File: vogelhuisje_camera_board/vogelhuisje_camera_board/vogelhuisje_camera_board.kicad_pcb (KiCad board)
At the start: 2 copper layers, 40 x 84 mm, 23 parts, among them J1 Conn_01x19_Female, J4 Camera Connector, Q2 Q_NMOS_DSG, U1 XC6206-2.8V, U2 XC6206-1.2V

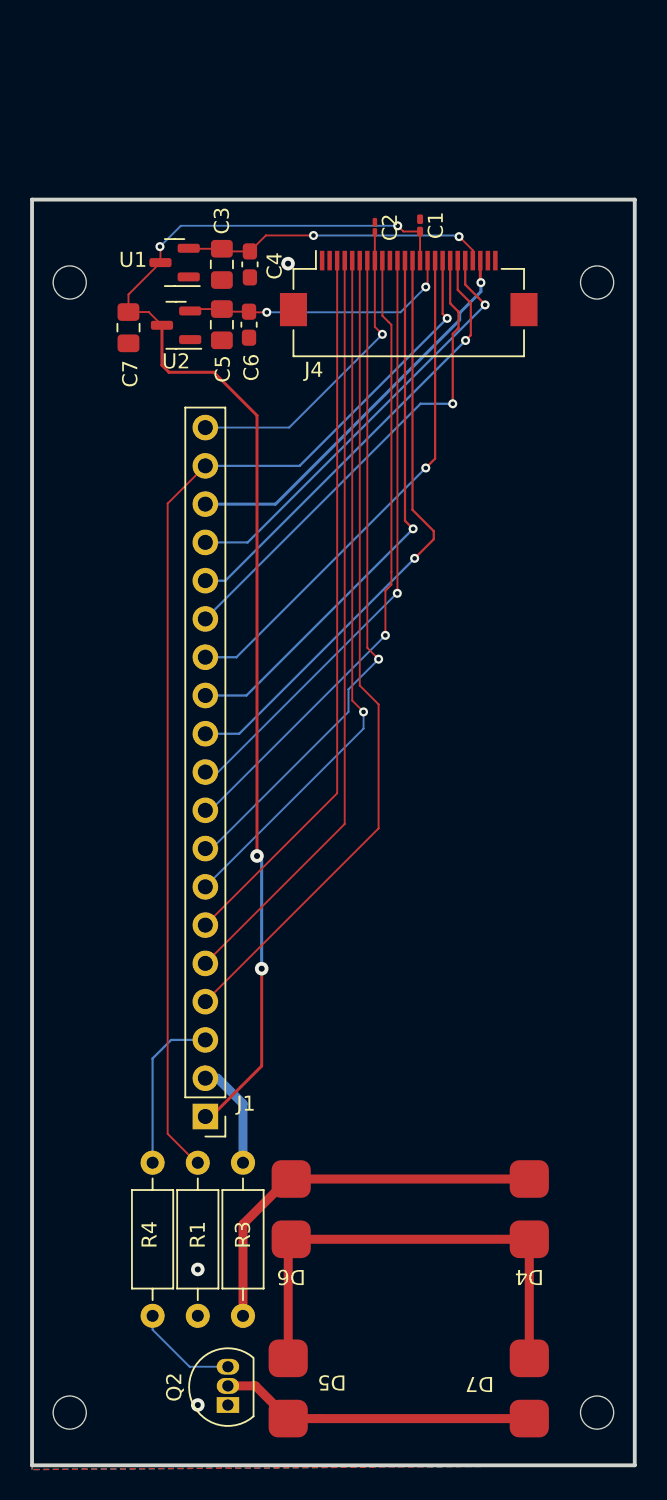
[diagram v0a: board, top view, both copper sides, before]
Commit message: Kicad Changes Tadjiro
Board now supports 3 lipo cells and a motion sensor.
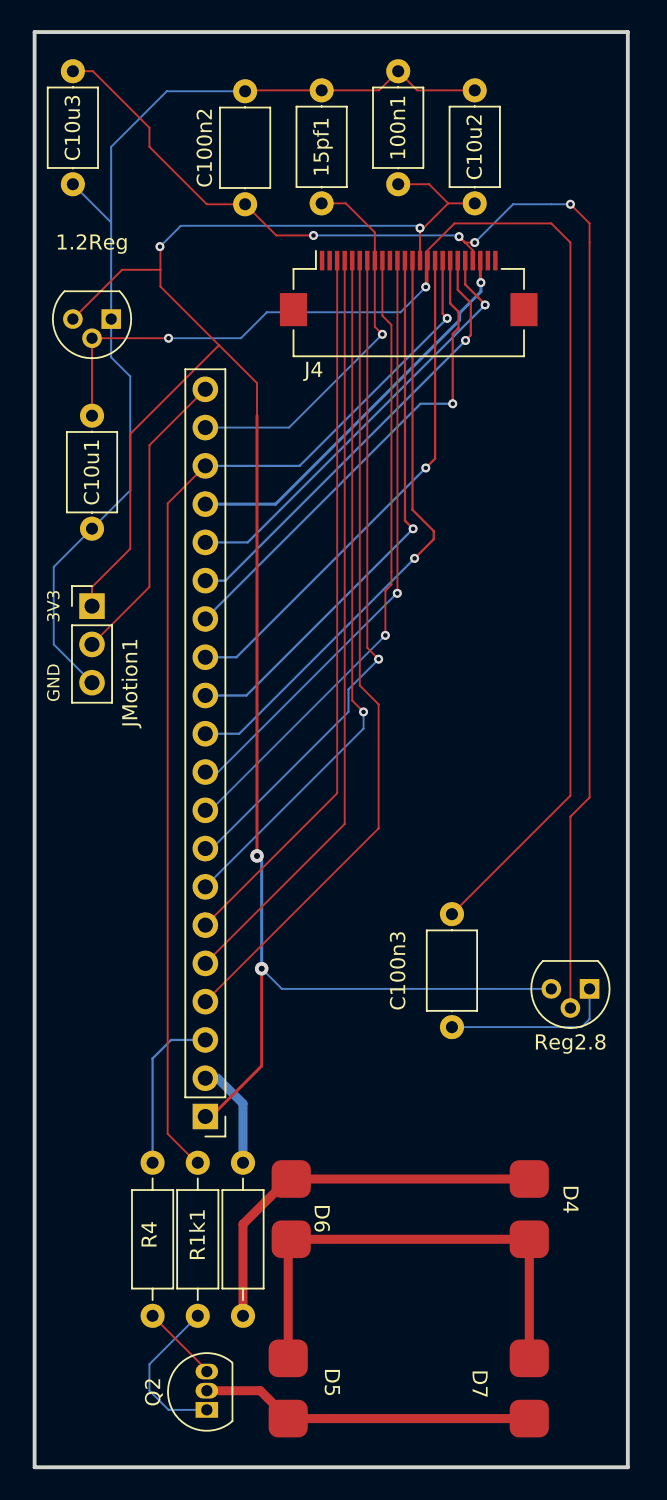
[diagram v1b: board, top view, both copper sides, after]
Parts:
- removed REF** (x4): MountingHole_2.2mm_M2, MountingHole:MountingHole_2.2mm_M2
- added JMotion1: Conn_01x03_Female, Connector_PinHeader_2.54mm:PinHeader_1x03_P2.54mm_Vertical, F.Cu at (94.0, 94.0)
- 1.2Reg: renamed from U2; value XC6206-1.2V -> 1.2V Regulator; footprint Package_TO_SOT_SMD:SOT-23 -> Package_TO_SOT_THT:TO-92
- 100n1: renamed from C1; value 100n -> 100nF; footprint Capacitor_SMD:C_0201_0603Metric_Pad0.64x0.40mm_HandSolder -> Capacitor_THT:C_Axial_L5.1mm_D3.1mm_P7.50mm_Horizontal
- 15pf1: renamed from C2; footprint Capacitor_SMD:C_01005_0402Metric_Pad0.57x0.30mm_HandSolder -> Capacitor_THT:C_Axial_L5.1mm_D3.1mm_P7.50mm_Horizontal
- C100n2: renamed from C4; footprint Capacitor_SMD:C_0603_1608Metric_Pad1.08x0.95mm_HandSolder -> Capacitor_THT:C_Axial_L5.1mm_D3.1mm_P7.50mm_Horizontal
- C100n3: renamed from C6; footprint Capacitor_SMD:C_0603_1608Metric_Pad1.08x0.95mm_HandSolder -> Capacitor_THT:C_Axial_L5.1mm_D3.1mm_P7.50mm_Horizontal
- C10u1: renamed from C5; footprint Capacitor_SMD:C_0805_2012Metric_Pad1.18x1.45mm_HandSolder -> Capacitor_THT:C_Axial_L5.1mm_D3.1mm_P7.50mm_Horizontal
- C10u2: renamed from C7; footprint Capacitor_SMD:C_0805_2012Metric_Pad1.18x1.45mm_HandSolder -> Capacitor_THT:C_Axial_L5.1mm_D3.1mm_P7.50mm_Horizontal
- C10u3: renamed from C3; footprint Capacitor_SMD:C_0805_2012Metric_Pad1.18x1.45mm_HandSolder -> Capacitor_THT:C_Axial_L5.1mm_D3.1mm_P7.50mm_Horizontal
- J1: value Conn_01x19_Female -> Conn_01x20_Female; footprint Connector_PinHeader_2.54mm:PinHeader_1x19_P2.54mm_Vertical -> Connector_PinHeader_2.54mm:PinHeader_1x20_P2.54mm_Vertical
- R1k1: renamed from R1; value 1k -> 1k1
- Reg2.8: renamed from U1; value XC6206-2.8V -> 2.8V regulator; footprint Package_TO_SOT_SMD:SOT-23 -> Package_TO_SOT_THT:TO-92
- moved Reg2.8 55.5 mm to (127.0, 119.4)
- moved C100n3 41.4 mm to (117.9, 114.4)
- moved C10u2 24.4 mm to (119.4, 67.2), turned to 90 degrees
- moved C10u3 16.2 mm to (92.7, 58.5)
- moved C10u1 10.5 mm to (94.0, 81.3)
- moved 100n1 10.3 mm to (114.3, 58.5)
- moved 15pf1 9.75 mm to (109.2, 59.8)
- moved 1.2Reg 4.33 mm to (95.2, 74.9)
- moved C100n2 4.00 mm to (104.1, 67.3), turned to 90 degrees
- moved Q2 1.44 mm to (101.6, 147.3)
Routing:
- net GND: track 0.00 -> 91.6 mm, vias 3 -> 0
- net CSI_2.8V: track 20.5 -> 95.9 mm, vias 2 -> 4
- net CSI_1.2V: track 18.3 -> 91.6 mm
- net 3V3: track 86.5 -> 138.1 mm
- net /Camera Module/Motion_out: track 0.00 -> 20.0 mm
- net /Camera Module/CSI_PCLK: track 21.3 -> 25.6 mm
- net Net-(Q2-Pad3): track 6.94 -> 5.19 mm
- net Net-(D5-Pad1): track 20.9 -> 22.2 mm
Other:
- board size 40 x 84 mm -> 39.4 x 95.2 mm
- board text added: "3V3"
- board text added: "GND"

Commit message: Updated Camera Board
Moved capacitors close to LDO output, corrected capacitor values and ported ground from the main board.
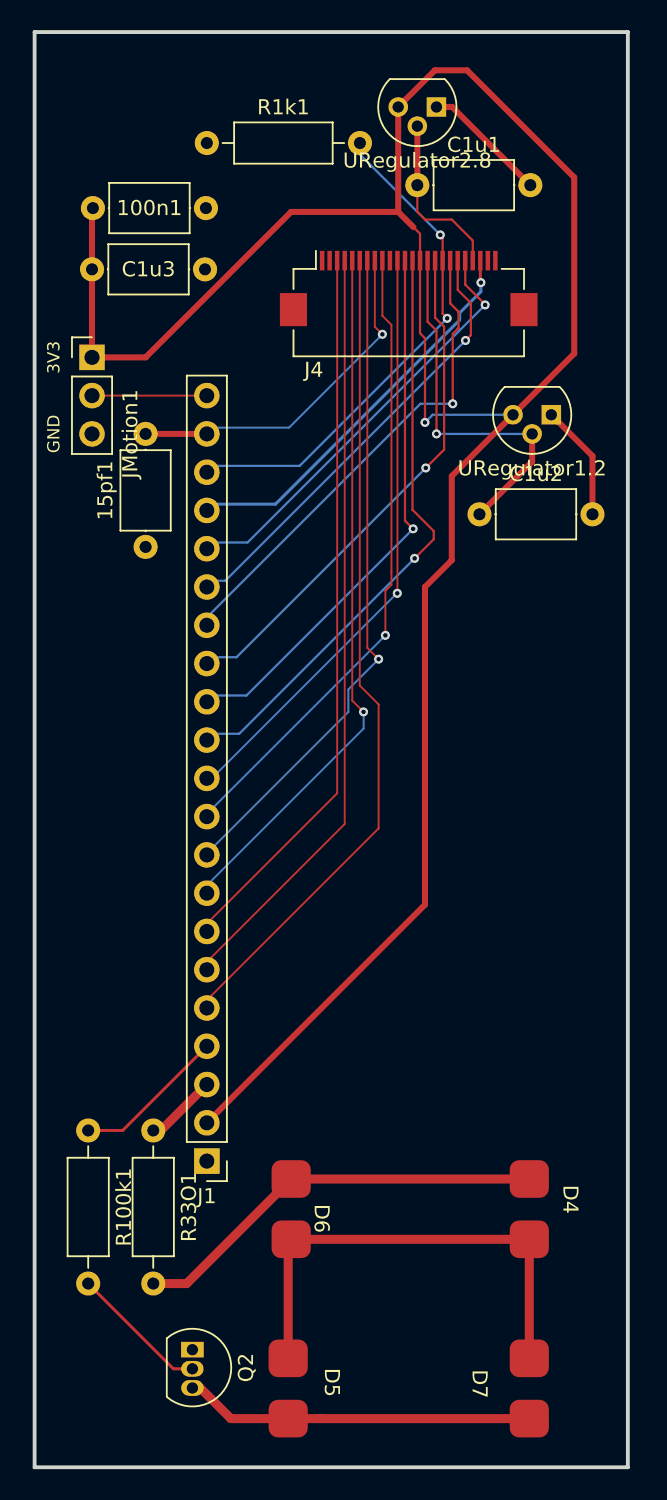
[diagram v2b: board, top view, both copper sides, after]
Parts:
- removed 1.2Reg: 1.2V Regulator, Package_TO_SOT_THT:TO-92
- removed C100n2, C100n3: 100n, Capacitor_THT:C_Axial_L5.1mm_D3.1mm_P7.50mm_Horizontal
- removed C10u1, C10u2, C10u3: 10u, Capacitor_THT:C_Axial_L5.1mm_D3.1mm_P7.50mm_Horizontal
- removed R3, R4: R, Resistor_THT:R_Axial_DIN0207_L6.3mm_D2.5mm_P10.16mm_Horizontal
- removed Reg2.8: 2.8V regulator, Package_TO_SOT_THT:TO-92
- added C1u1: 1u, Capacitor_THT:C_Axial_L5.1mm_D3.1mm_P7.50mm_Horizontal, F.Cu at (115.6, 66.0)
- added C1u2: 1u, Capacitor_THT:C_Axial_L5.1mm_D3.1mm_P7.50mm_Horizontal, F.Cu at (119.7, 87.9)
- added C1u3: 1u, Capacitor_THT:C_Axial_L5.1mm_D3.1mm_P7.50mm_Horizontal, F.Cu at (94.0, 71.6)
- added R100k1: 100kOhm, Resistor_THT:R_Axial_DIN0207_L6.3mm_D2.5mm_P10.16mm_Horizontal, F.Cu at (93.7, 128.8)
- added R33O1: 33Ohm, Resistor_THT:R_Axial_DIN0207_L6.3mm_D2.5mm_P10.16mm_Horizontal, F.Cu at (98.0, 128.8)
- added URegulator1.2: 1.2V Regulator, Package_TO_SOT_THT:TO-92, F.Cu at (124.5, 81.3)
- added URegulator2.8: 2.8V regulator, Package_TO_SOT_THT:TO-92, F.Cu at (116.8, 60.9)
- J1: value Conn_01x20_Female -> Conn_01x21_Female; footprint Connector_PinHeader_2.54mm:PinHeader_1x20_P2.54mm_Vertical -> Connector_PinHeader_2.54mm:PinHeader_1x21_P2.54mm_Vertical
- Q2: value Q_NMOS_DSG -> Q_NMOS_DGS
- moved R1k1 77.8 mm to (101.6, 63.2), turned to 0 degrees
- moved 15pf1 32.5 mm to (97.5, 90.0), turned to 90 degrees
- moved JMotion1 16.5 mm to (94.0, 77.5)
- moved 100n1 15.7 mm to (101.5, 67.6), turned to 180 degrees
- moved Q2 4.11 mm to (100.6, 143.3), turned to -90 degrees
- moved J1 2.96 mm to (101.6, 130.8)
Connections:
- J1 pad 1: 3V3 -> GND
- J1 pad 10: /Camera Module/CSI_D6 -> /Camera Module/CSI_D5
- J1 pad 11: /Camera Module/CSI_D7 -> /Camera Module/CSI_D6
- J1 pad 12: /Camera Module/CSI_MCLK -> /Camera Module/CSI_D7
- J1 pad 13: /Camera Module/CSI_HSYNC -> /Camera Module/CSI_MCLK
- J1 pad 14: /Camera Module/CSI_VSYNC -> /Camera Module/CSI_HSYNC
- J1 pad 15: /Camera Module/CAM_RST -> /Camera Module/CSI_VSYNC
- J1 pad 16: /Camera Module/TWI_SCK -> /Camera Module/CAM_RST
- J1 pad 17: /Camera Module/TWI_SDA -> /Camera Module/TWI_SCK
- J1 pad 18: /Camera Module/PWDN -> /Camera Module/TWI_SDA
- J1 pad 19: /Camera Module/CSI_PCLK -> /Camera Module/PWDN
- J1 pad 2: /Camera Module/Vbat -> 3V3
- J1 pad 20: /Camera Module/Motion_out -> /Camera Module/CSI_PCLK
- J1 pad 3: /Camera Module/V_led_switch- -> /Camera Module/Vbat
- J1 pad 4: /Camera Module/CSI_D0 -> /Camera Module/V_led_switch-
- J1 pad 5: /Camera Module/CSI_D1 -> /Camera Module/CSI_D0
- J1 pad 6: /Camera Module/CSI_D2 -> /Camera Module/CSI_D1
- J1 pad 7: /Camera Module/CSI_D3 -> /Camera Module/CSI_D2
- J1 pad 8: /Camera Module/CSI_D4 -> /Camera Module/CSI_D3
- J1 pad 9: /Camera Module/CSI_D5 -> /Camera Module/CSI_D4
- Q2 pad 2: Net-(D5-Pad1) -> Net-(Q2-Pad2)
- Q2 pad 3: Net-(Q2-Pad3) -> Net-(D5-Pad1)
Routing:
- net CSI_2.8V: track 95.9 -> 11.5 mm, vias 4 -> 0
- net GND: track 91.6 -> 16.1 mm
- net CSI_1.2V: track 91.6 -> 24.9 mm, vias 2 -> 1
- net /Camera Module/PWDN: track 72.2 -> 34.1 mm, vias 1 -> 2
- net 3V3: track 138.1 -> 150.8 mm, vias 4 -> 1
- net /Camera Module/Motion_out: track 20.0 -> 7.62 mm
- net Net-(Q2-Pad2): track 0.00 -> 9.26 mm
- net Net-(Q2-Pad3): track 5.19 -> 0.00 mm
- net /Camera Module/Vbat: track 7.12 -> 4.82 mm
- net /Camera Module/CSI_PCLK: track 25.6 -> 23.5 mm
- net Net-(D4-Pad2): track 26.3 -> 28.0 mm
- net Net-(D5-Pad1): track 22.2 -> 23.2 mm
- net /Camera Module/V_led_switch-: track 10.9 -> 10.2 mm

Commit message: Old changes reuploaded
Weird thing happened with git pushes. Hopefully this will solve the problems
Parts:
- added R100k2: 100kOhm, Resistor_THT:R_Axial_DIN0207_L6.3mm_D2.5mm_P10.16mm_Horizontal, F.Cu at (102.6, 59.9)
- added R100k3: 100kOhm, Resistor_THT:R_Axial_DIN0207_L6.3mm_D2.5mm_P10.16mm_Horizontal, F.Cu at (119.6, 91.9)
- moved 15pf1 1.33 mm to (97.5, 91.4)
- moved JMotion1 0.25 mm to (93.7, 77.5)
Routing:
- net CSI_2.8V: track 11.5 -> 25.3 mm
- net CSI_1.2V: track 24.9 -> 28.9 mm
- net /Camera Module/CSI_PCLK: track 23.5 -> 24.0 mm
